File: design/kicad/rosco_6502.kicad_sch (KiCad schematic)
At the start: 52 parts, among them IC1 W65C02SxP, IC2 ATF22V10C-7PX, IC3 XR68C681CJTR-F, IC4 NE555P, IC5 ATF22V10C-7PX, J1 UART_A, J2 UART_B, J3 Conn_01x06, J4 Conn_01x01_Male, J5 Conn_02x18_Odd_Even, Q1 3.6864MHz, SW1 SW_DPST, U1 AS6C4008-55PCN, U2 AS6C62256-55PCN, U3 AT28C64B-15PU, U4 74HCT174, X1 14MHz

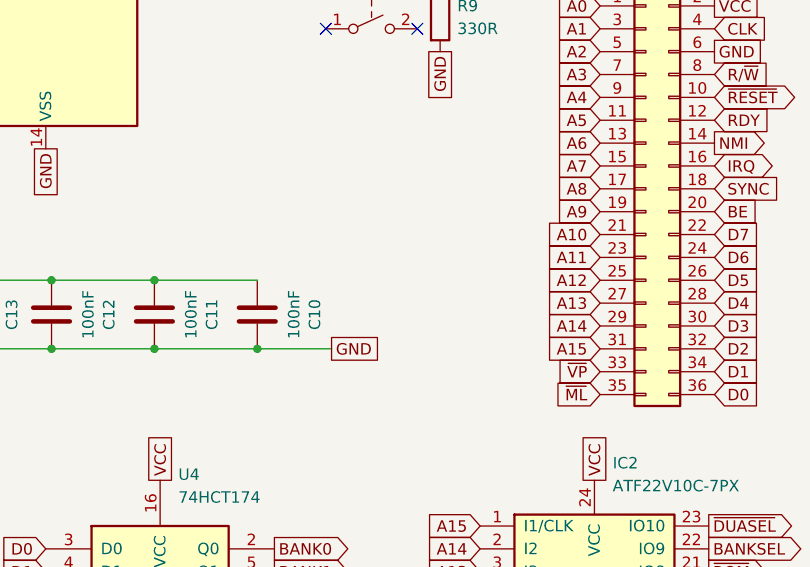
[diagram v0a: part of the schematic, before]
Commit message: Power connector & silk update
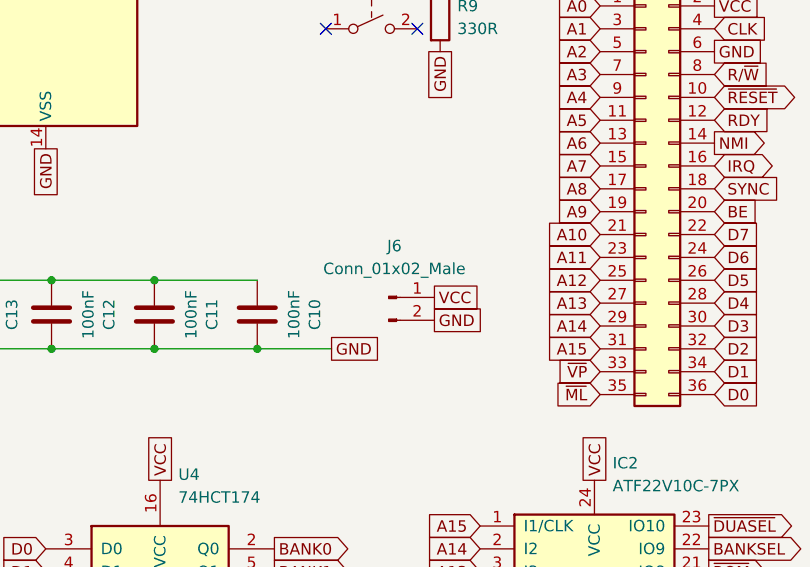
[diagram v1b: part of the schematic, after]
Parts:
- added J6: Conn_01x02_Male, Connector_PinHeader_2.54mm:PinHeader_1x02_P2.54mm_Vertical, symbol Connector:Conn_01x02_Male
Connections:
- net GND: now also J6.2 (Pin_2)
- net VCC: now also J6.1 (Pin_1)
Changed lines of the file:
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@@
+    )
+  )
+  (global_label "GND" (shape passive) (at 238.125 97.155 0) (fields_autoplaced)
+    (effects (font (size 1.27 1.27)) (justify left))
+    (property "Intersheet References" "${INTERSHEET_REFS}" (id 0) (at 244.4086 97.0756 0)
+      (effects (font (size 1.27 1.27)) (justify left) hide)
     )
   )
@@
     (property "Intersheet References" "${INTERSHEET_REFS}" (id 0) (at 256.4606 51.3686 90)
       (effects (font (size 1.27 1.27)) (justify right) hide)
+    )
+  )
+  (global_label "VCC" (shape passive) (at 238.125 94.615 0) (fields_autoplaced)
+    (effects (font (size 1.27 1.27)) (justify left))
+    (property "Intersheet References" "${INTERSHEET_REFS}" (id 0) (at 244.1667 94.5356 0)
+      (effects (font (size 1.27 1.27)) (justify left) hide)
     )
   )
@@
     (pin "8")
     (pin "9")
+  )
+  (symbol (lib_id "Connector:Conn_01x02_Male") (at 233.045 94.615 0) (unit 1)
+    (in_bom yes) (on_board yes) (fields_autoplaced)
+    (property "Reference" "J6" (id 0) (at 233.68 88.9 0))
+    (property "Value" "Conn_01x02_Male" (id 1) (at 233.68 91.44 0))
+    (property "Footprint" "Connector_PinHeader_2.54mm:PinHeader_1x02_P2.54mm_Vertical" (id 2) (at 233.045 94.615 0)
+      (effects (font (size 1.27 1.27)) hide)
+    )
+    (property "Datasheet" "~" (id 3) (at 233.045 94.615 0)
+      (effects (font (size 1.27 1.27)) hide)
+    )
+    (pin "1")
+    (pin "2")
   )
   (symbol (lib_id "Jumper:Jumper_2_Open") (at 60.325 193.04 0) (unit 1)
@@
       (reference "J5") (unit 1) (value "Conn_02x18_Odd_Even") (footprint "Connector_PinHeader_2.54mm:PinHeader_2x18_P2.54mm_Vertical")
     )
+    (path "/49dd41aa-f677-45d8-941f-226f9b63a72f"
+      (reference "J6") (unit 1) (value "Conn_01x02_Male") (footprint "Connector_PinHeader_2.54mm:PinHeader_1x02_P2.54mm_Vertical")
+    )
     (path "/95aa87c4-9825-4d0e-9c7f-43fd315f0e3c"

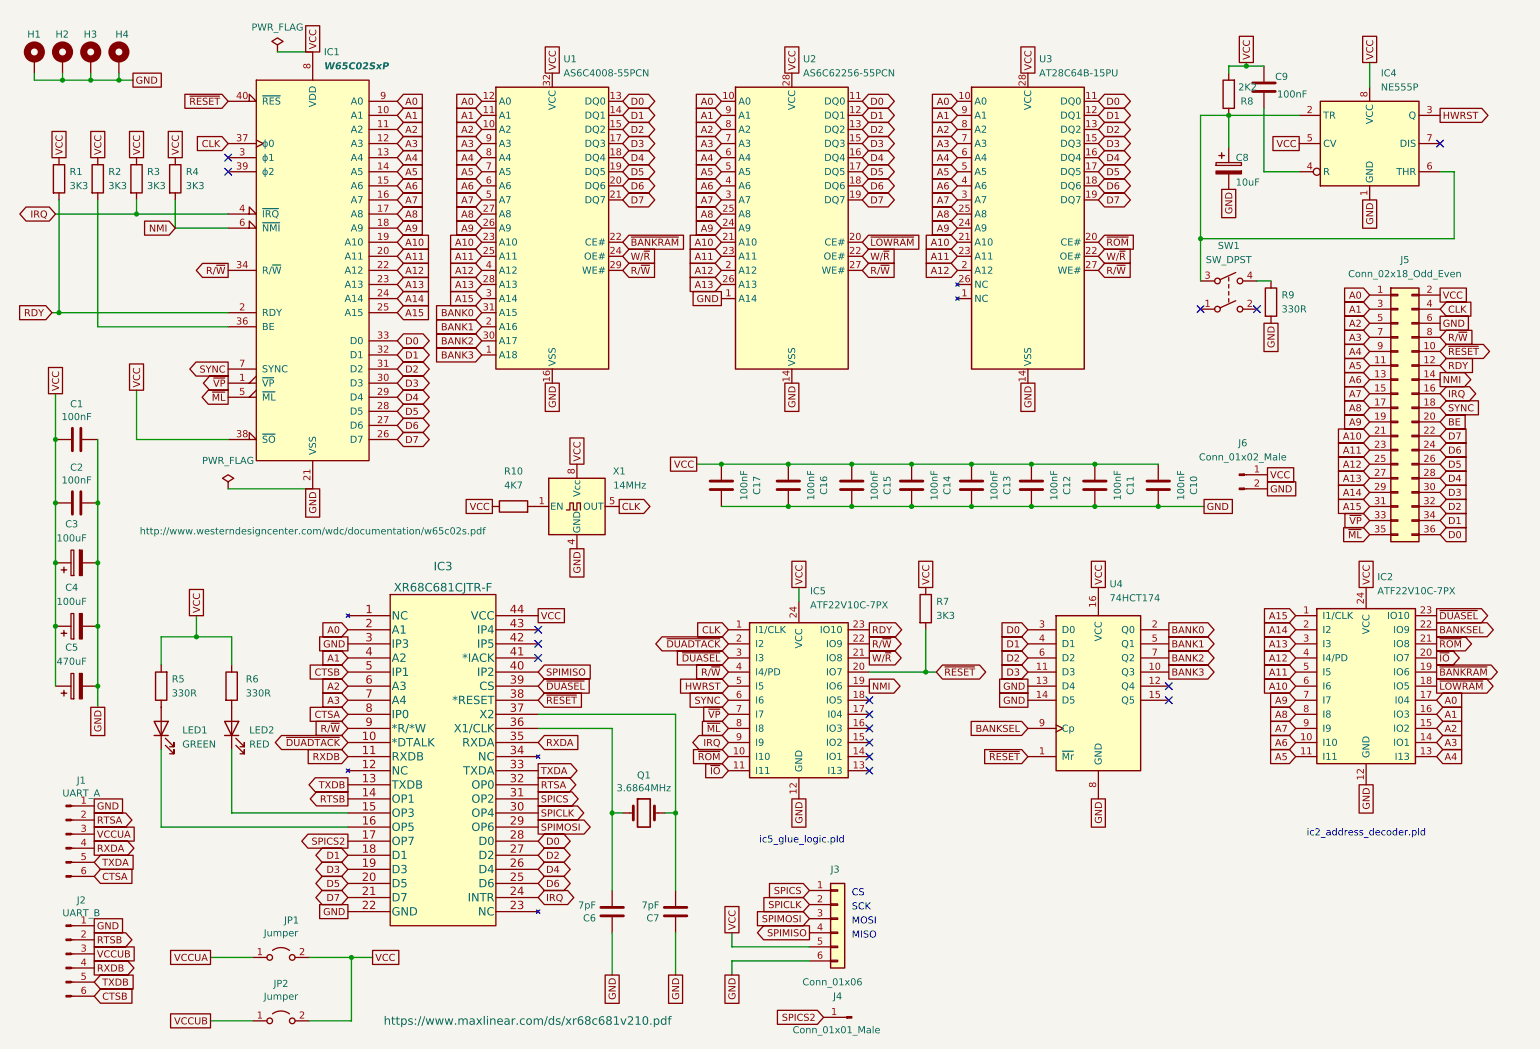
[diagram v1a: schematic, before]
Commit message: Add CLK into RD/WR and reroute
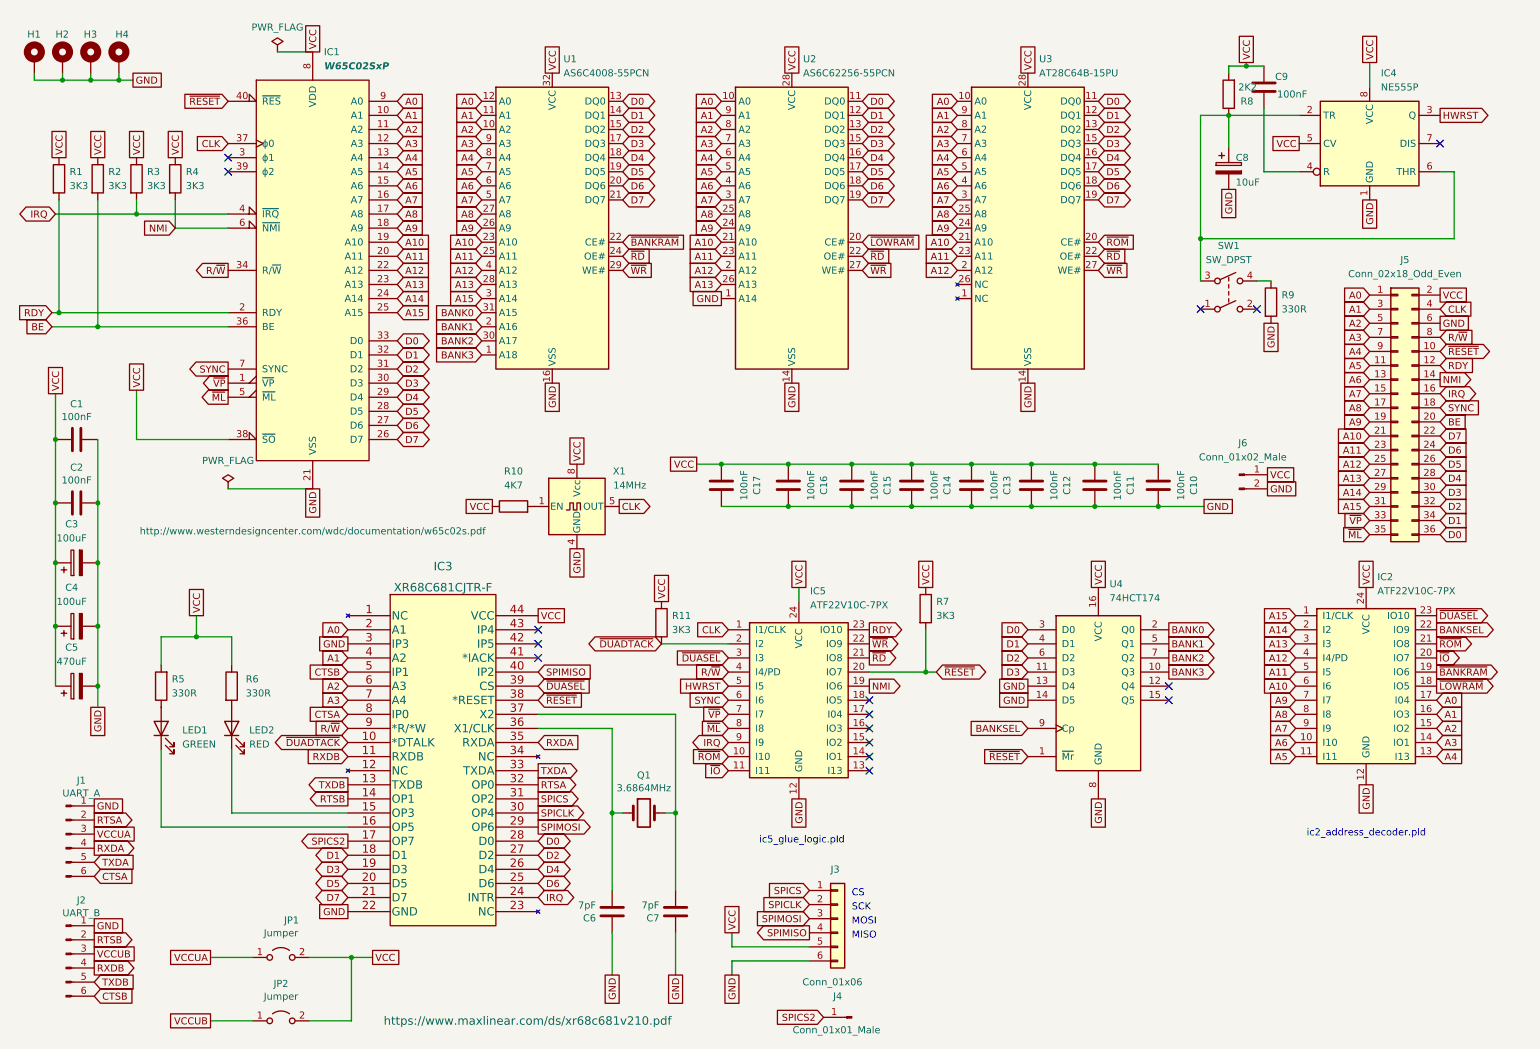
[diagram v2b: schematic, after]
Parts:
- added R11: 3K3, Resistor_THT:R_Axial_DIN0207_L6.3mm_D2.5mm_P10.16mm_Horizontal, symbol Device:R
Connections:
- net BE: now also IC1.36 (BE), R2.2
- net R/~{W}: no longer IC5.22 (IO9), U1.29 (WE#), U2.27 (WE#), U3.27 (WE#)
- net VCC: now also R11.1
- net ~{DUADTACK}: now also R11.2
- net W/~{R} renamed ~{RD}
- new net ~{WR}: IC5.22 (IO9), U1.29 (WE#), U2.27 (WE#), U3.27 (WE#)
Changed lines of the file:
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@@
   (junction (at 207.01 100.33) (diameter 0) (color 0 0 0 0)
   )
+  (junction (at 27.305 67.945) (diameter 0) (color 0 0 0 0)
+  )
   (junction (at 45.085 123.825) (diameter 0) (color 0 0 0 0)
   )
@@
     (stroke (width 0) (type default) (color 0 0 0 0))
   )
+  (wire (pts (xy 128.905 125.095) (xy 140.97 125.095))
+    (stroke (width 0) (type default) (color 0 0 0 0))
+  )
   (wire (pts (xy 184.785 92.71) (xy 173.99 92.71))
     (stroke (width 0) (type default) (color 0 0 0 0))
@@
     (stroke (width 0) (type default) (color 0 0 0 0))
   )
+  (wire (pts (xy 19.05 67.945) (xy 27.305 67.945))
+    (stroke (width 0) (type default) (color 0 0 0 0))
+  )
   (wire (pts (xy 31.115 22.225) (xy 31.115 23.495))
     (stroke (width 0) (type default) (color 0 0 0 0))
@@
     )
   )
+  (global_label "BE" (shape input) (at 19.05 67.945 180) (fields_autoplaced)
+    (effects (font (size 1.27 1.27)) (justify right))
+    (property "Intersheet References" "${INTERSHEET_REFS}" (id 0) (at 14.2179 67.8656 0)
+      (effects (font (size 1.27 1.27)) (justify right) hide)
+    )
+  )
   (global_label "A15" (shape input) (at 81.28 65.405 0) (fields_autoplaced)
     (effects (font (size 1.27 1.27)) (justify left))
@@
     )
   )
-  (global_label "R{slash}~{W}" (shape input) (at 121.92 57.785 0) (fields_autoplaced)
+  (global_label "~{WR}" (shape input) (at 121.92 57.785 0) (fields_autoplaced)
     (effects (font (size 1.27 1.27)) (justify left))
-    (property "Intersheet References" "${INTERSHEET_REFS}" (id 0) (at 128.385 57.7056 0)
+    (property "Intersheet References" "${INTERSHEET_REFS}" (id 0) (at 127.0545 57.7056 0)
       (effects (font (size 1.27 1.27)) (justify left) hide)
     )
@@
     )
   )
-  (global_label "W{slash}~{R}" (shape input) (at 121.92 55.245 0) (fields_autoplaced)
+  (global_label "~{RD}" (shape input) (at 121.92 55.245 0) (fields_autoplaced)
     (effects (font (size 1.27 1.27)) (justify left))
-    (property "Intersheet References" "${INTERSHEET_REFS}" (id 0) (at 128.385 55.1656 0)
+    (property "Intersheet References" "${INTERSHEET_REFS}" (id 0) (at 126.8731 55.1656 0)
       (effects (font (size 1.27 1.27)) (justify left) hide)
     )
@@
     )
   )
-  (global_label "W{slash}~{R}" (shape input) (at 165.1 55.245 0) (fields_autoplaced)
+  (global_label "~{RD}" (shape input) (at 165.1 55.245 0) (fields_autoplaced)
     (effects (font (size 1.27 1.27)) (justify left))
-    (property "Intersheet References" "${INTERSHEET_REFS}" (id 0) (at 171.565 55.1656 0)
+    (property "Intersheet References" "${INTERSHEET_REFS}" (id 0) (at 170.0531 55.1656 0)
       (effects (font (size 1.27 1.27)) (justify left) hide)
     )
@@
     )
   )
-  (global_label "R{slash}~{W}" (shape output) (at 166.37 125.095 0) (fields_autoplaced)
+  (global_label "~{WR}" (shape output) (at 166.37 125.095 0) (fields_autoplaced)
     (effects (font (size 1.27 1.27)) (justify left))
-    (property "Intersheet References" "${INTERSHEET_REFS}" (id 0) (at 172.835 125.0156 0)
+    (property "Intersheet References" "${INTERSHEET_REFS}" (id 0) (at 171.5045 125.0156 0)
       (effects (font (size 1.27 1.27)) (justify left) hide)
     )
@@
     )
   )
-  (global_label "R{slash}~{W}" (shape input) (at 165.1 57.785 0) (fields_autoplaced)
+  (global_label "~{WR}" (shape input) (at 165.1 57.785 0) (fields_autoplaced)
     (effects (font (size 1.27 1.27)) (justify left))
-    (property "Intersheet References" "${INTERSHEET_REFS}" (id 0) (at 171.565 57.7056 0)
+    (property "Intersheet References" "${INTERSHEET_REFS}" (id 0) (at 170.2345 57.7056 0)
       (effects (font (size 1.27 1.27)) (justify left) hide)
     )
@@
     )
   )
-  (global_label "W{slash}~{R}" (shape input) (at 207.645 55.245 0) (fields_autoplaced)
+  (global_label "~{RD}" (shape input) (at 207.645 55.245 0) (fields_autoplaced)
     (effects (font (size 1.27 1.27)) (justify left))
-    (property "Intersheet References" "${INTERSHEET_REFS}" (id 0) (at 214.11 55.1656 0)
+    (property "Intersheet References" "${INTERSHEET_REFS}" (id 0) (at 212.5981 55.1656 0)
       (effects (font (size 1.27 1.27)) (justify left) hide)
     )
@@
     )
   )
-  (global_label "~{DUADTACK}" (shape tri_state) (at 140.97 125.095 180) (fields_autoplaced)
+  (global_label "~{DUADTACK}" (shape tri_state) (at 128.905 125.095 180) (fields_autoplaced)
     (effects (font (size 1.27 1.27)) (justify right))
-    (property "Intersheet References" "${INTERSHEET_REFS}" (id 0) (at 129.0017 125.0156 0)
+    (property "Intersheet References" "${INTERSHEET_REFS}" (id 0) (at 116.9367 125.0156 0)
       (effects (font (size 1.27 1.27)) (justify right) hide)
     )
@@
     )
   )
-  (global_label "W{slash}~{R}" (shape output) (at 166.37 127.635 0) (fields_autoplaced)
+  (global_label "~{RD}" (shape output) (at 166.37 127.635 0) (fields_autoplaced)
     (effects (font (size 1.27 1.27)) (justify left))
-    (property "Intersheet References" "${INTERSHEET_REFS}" (id 0) (at 172.835 127.5556 0)
+    (property "Intersheet References" "${INTERSHEET_REFS}" (id 0) (at 171.3231 127.5556 0)
       (effects (font (size 1.27 1.27)) (justify left) hide)
     )
@@
     )
   )
-  (global_label "R{slash}~{W}" (shape input) (at 207.645 57.785 0) (fields_autoplaced)
+  (global_label "~{WR}" (shape input) (at 207.645 57.785 0) (fields_autoplaced)
     (effects (font (size 1.27 1.27)) (justify left))
-    (property "Intersheet References" "${INTERSHEET_REFS}" (id 0) (at 214.11 57.7056 0)
+    (property "Intersheet References" "${INTERSHEET_REFS}" (id 0) (at 212.7795 57.7056 0)
       (effects (font (size 1.27 1.27)) (justify left) hide)
     )
@@
     )
   )
+  (global_label "VCC" (shape passive) (at 128.905 117.475 90) (fields_autoplaced)
+    (effects (font (size 1.27 1.27)) (justify left))
+    (property "Intersheet References" "${INTERSHEET_REFS}" (id 0) (at 128.8256 111.4333 90)
+      (effects (font (size 1.27 1.27)) (justify left) hide)
+    )
+  )
   (global_label "GND" (shape passive) (at 26.67 154.305 0) (fields_autoplaced)
     (effects (font (size 1.27 1.27)) (justify left))
@@
     (pin "2")
   )
+  (symbol (lib_id "Device:R") (at 128.905 121.285 0) (unit 1)
+    (in_bom yes) (on_board yes) (fields_autoplaced)
+    (property "Reference" "R11" (id 0) (at 130.81 120.0149 0)
+      (effects (font (size 1.27 1.27)) (justify left))
+    )
+    (property "Value" "3K3" (id 1) (at 130.81 122.5549 0)
+      (effects (font (size 1.27 1.27)) (justify left))
+    )
+    (property "Footprint" "Resistor_THT:R_Axial_DIN0207_L6.3mm_D2.5mm_P10.16mm_Horizontal" (id 2) (at 127.127 121.285 90)
+      (effects (font (size 1.27 1.27)) hide)
+    )
+    (property "Datasheet" "~" (id 3) (at 128.905 121.285 0)
+      (effects (font (size 1.27 1.27)) hide)
+    )
+    (pin "1")
+    (pin "2")
+  )
   (symbol (lib_id "Device:C") (at 237.49 24.765 0) (unit 1)
     (in_bom yes) (on_board yes)
@@
       (reference "R10") (unit 1) (value "4K7") (footprint "Resistor_THT:R_Axial_DIN0207_L6.3mm_D2.5mm_P10.16mm_Horizontal")
     )
+    (path "/f5dcec41-5ab5-44ff-9edb-8c415c1256fa"
+      (reference "R11") (unit 1) (value "3K3") (footprint "Resistor_THT:R_Axial_DIN0207_L6.3mm_D2.5mm_P10.16mm_Horizontal")
+    )
     (path "/0d61b5ac-4ff5-4ae4-a1de-fa50189d2dac"

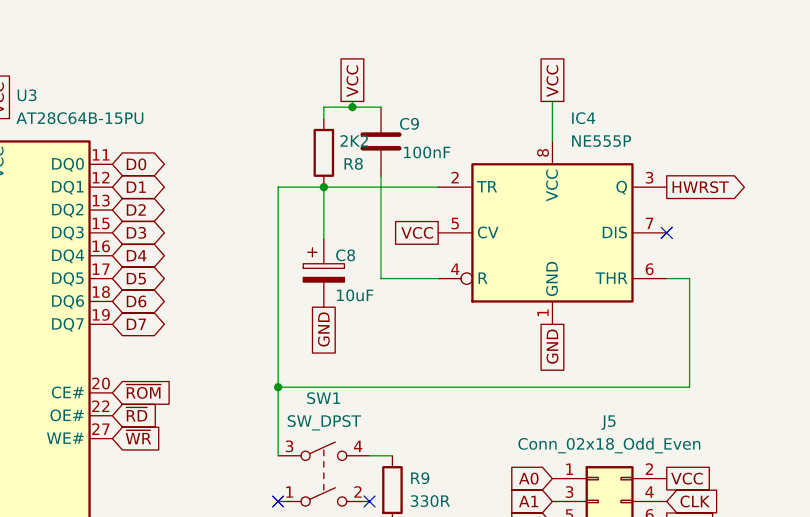
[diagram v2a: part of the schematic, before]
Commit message: Fix incorrect 555 hookup
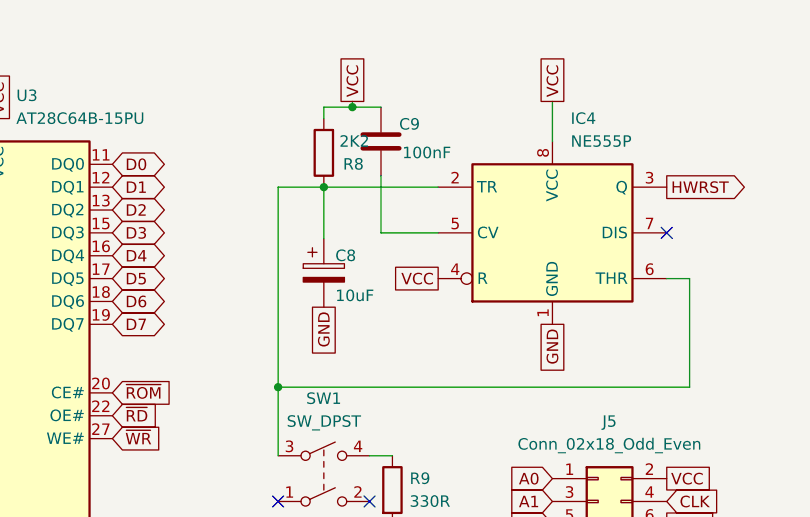
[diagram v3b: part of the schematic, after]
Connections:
- net VCC: now also IC4.4 (R); no longer IC4.5 (CV)
- net at C9.2: now also IC4.5 (CV); no longer IC4.4 (R)
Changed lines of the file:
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@@
-    (stroke (width 0) (type default) (color 0 0 0 0))
-  )
-  (wire (pts (xy 237.49 28.575) (xy 237.49 40.005))
     (stroke (width 0) (type default) (color 0 0 0 0))
   )
@@
     (stroke (width 0) (type default) (color 0 0 0 0))
   )
+  (wire (pts (xy 237.49 28.575) (xy 237.49 34.925))
+    (stroke (width 0) (type default) (color 0 0 0 0))
+  )
   (wire (pts (xy 231.14 29.845) (xy 231.14 35.56))
     (stroke (width 0) (type default) (color 0 0 0 0))
@@
     (stroke (width 0) (type default) (color 0 0 0 0))
   )
-  (wire (pts (xy 237.49 40.005) (xy 243.84 40.005))
-    (stroke (width 0) (type default) (color 0 0 0 0))
-  )
   (wire (pts (xy 184.785 100.33) (xy 173.99 100.33))
     (stroke (width 0) (type default) (color 0 0 0 0))
@@
   )
   (wire (pts (xy 19.685 121.92) (xy 19.685 132.715))
+    (stroke (width 0) (type default) (color 0 0 0 0))
+  )
+  (wire (pts (xy 237.49 34.925) (xy 243.84 34.925))
     (stroke (width 0) (type default) (color 0 0 0 0))
   )
@@
     )
   )
-  (global_label "VCC" (shape passive) (at 243.84 34.925 180) (fields_autoplaced)
-    (effects (font (size 1.27 1.27)) (justify right))
-    (property "Intersheet References" "${INTERSHEET_REFS}" (id 0) (at 237.7983 34.8456 0)
-      (effects (font (size 1.27 1.27)) (justify right) hide)
-    )
+  (global_label "VCC" (shape passive) (at 243.84 40.005 180) (fields_autoplaced)
+    (effects (font (size 1.27 1.27)) (justify right))
+    (property "Intersheet References" "${INTERSHEET_REFS}" (id 0) (at 237.7983 39.9256 0)
+      (effects (font (size 1.27 1.27)) (justify right) hide)
+    )
